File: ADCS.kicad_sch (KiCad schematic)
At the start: 14 parts

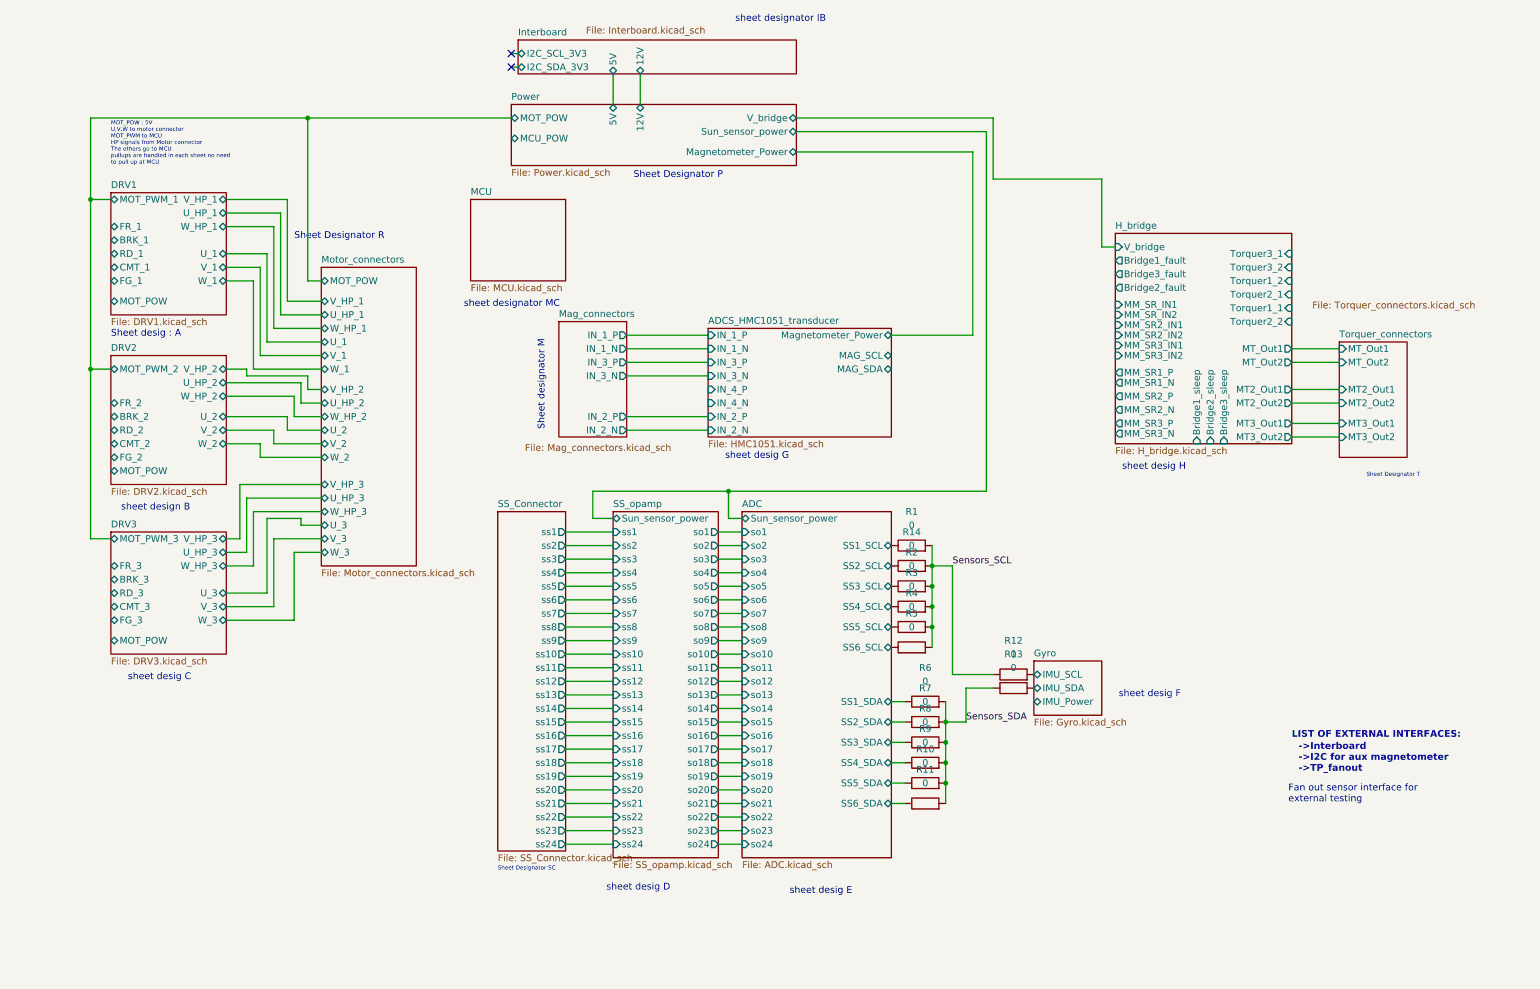
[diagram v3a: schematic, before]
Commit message: MCU interfaces pulled out to parent sheet
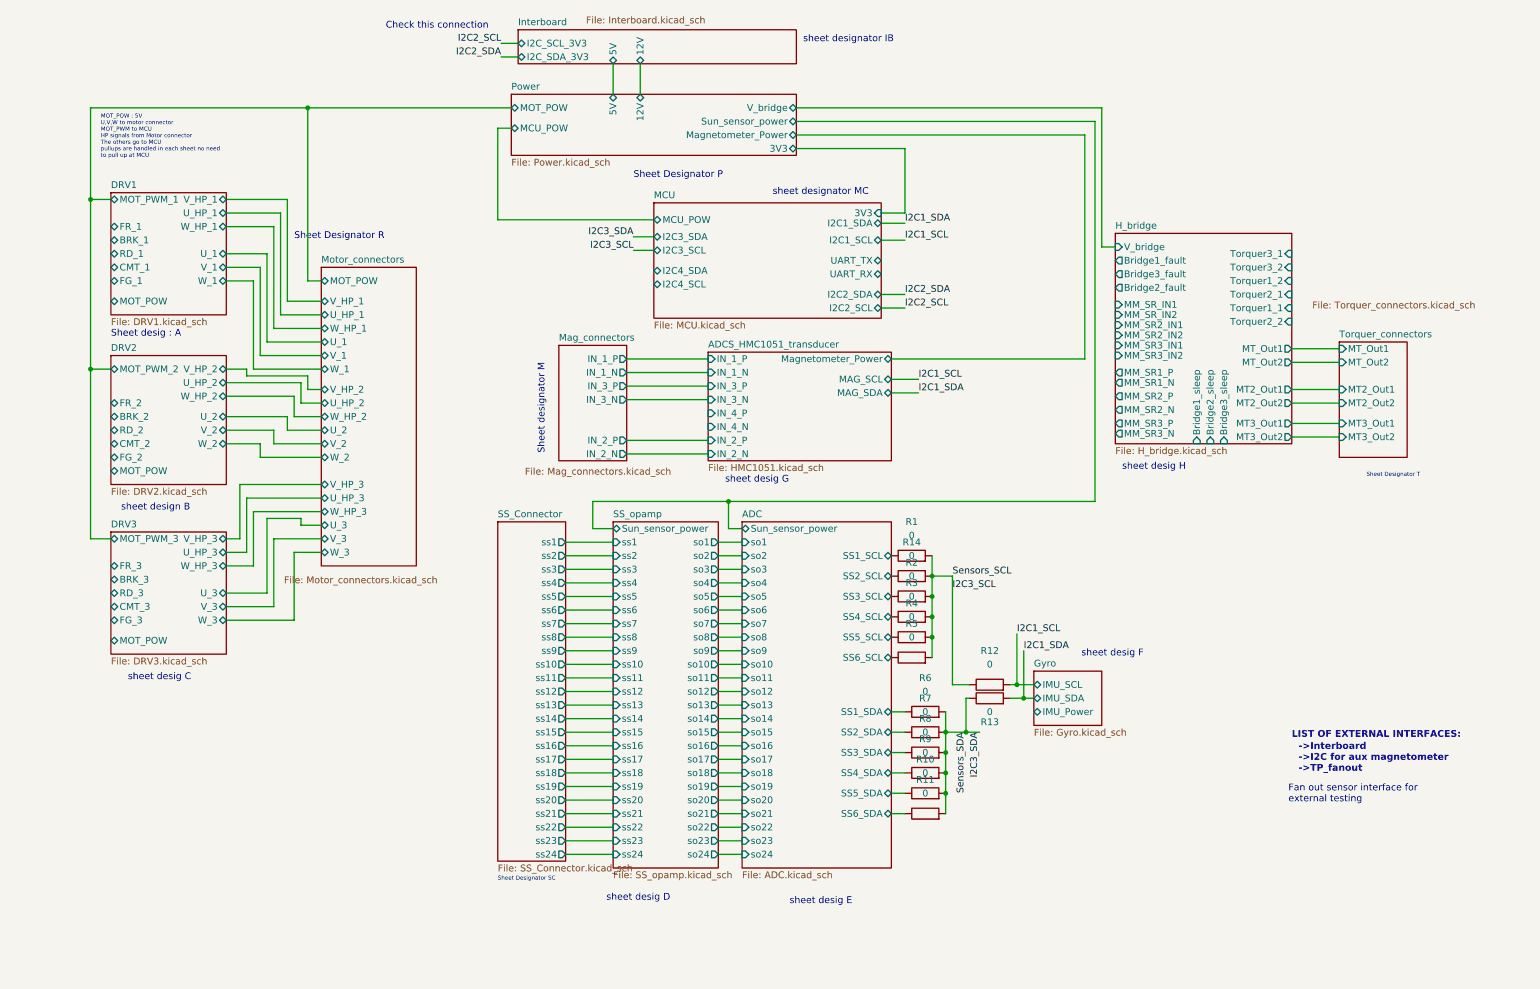
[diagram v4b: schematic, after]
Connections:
- net Gyro/IMU_SCL renamed I2C1_SCL
- net Gyro/IMU_SDA renamed I2C1_SDA
- net Sensors_SCL renamed I2C3_SCL
- net Sensors_SDA renamed I2C3_SDA
- no-connect marks 2 -> 0
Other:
- sheet MCU ports: added 3V3, I2C1_SCL, I2C1_SDA, I2C2_SCL, I2C2_SDA, I2C3_SCL, I2C3_SDA, I2C4_SCL, I2C4_SDA, MCU_POW, UART_RX, UART_TX; removed none
- sheet Power ports: added 3V3; removed none
- note added: "Check this connection"
- moved on the sheet: R1, R10, R11, R12, R13, R14, R2, R3, R4, R5, R6, R7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

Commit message: MCU interfaces are done! Check the Changes and Complete ERC modifications
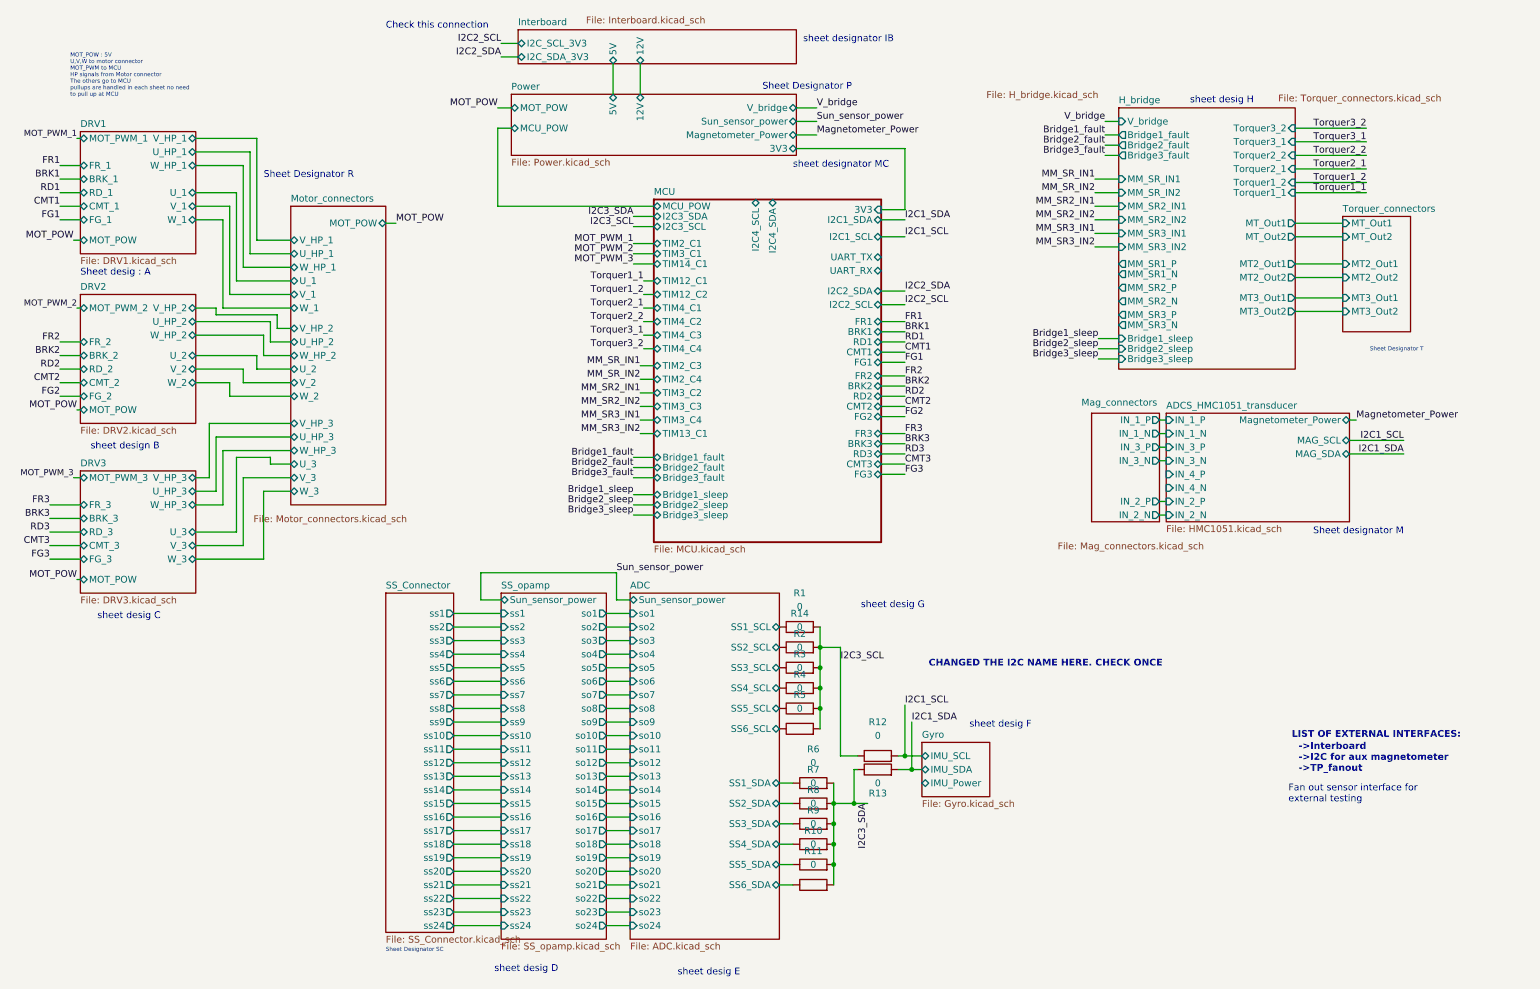
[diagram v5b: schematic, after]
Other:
- sheet MCU ports: added BRK1, BRK2, BRK3, Bridge1_fault, Bridge1_sleep, Bridge2_fault, Bridge2_sleep, Bridge3_fault, Bridge3_sleep, CMT1, CMT2, CMT3, FG1, FG2, FG3, FR1, FR2, FR3, RD1, RD2, RD3, TIM12_C1, TIM12_C2, TIM13_C1, TIM14_C1, TIM2_C1, TIM2_C3, TIM2_C4, TIM3_C1, TIM3_C2, TIM3_C3, TIM3_C4, TIM4_C1, TIM4_C2, TIM4_C3, TIM4_C4; removed none
- note added: "CHANGED THE I2C NAME HERE. CHECK ONCE"
- company: (none) -> Parikshit Student Satellite Team
- title: (none) -> AOCS BOARD
- moved on the sheet: R1, R10, R11, R12, R13, R14, R2, R3, R4, R5, R6, R7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

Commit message: added notes
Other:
- note added: "PWR flag for each power port ?"
- note added: "Please add necessary pull-ups for sensor buses Check each sheet for required pullups"
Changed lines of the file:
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@@
+    (effects (font (size 1.27 1.27)) (justify left bottom))
+  )
+  (text "PWR flag for each power port ? " (at 21.59 177.8 0)
     (effects (font (size 1.27 1.27)) (justify left bottom))
   )
@@
     (effects (font (size 0.762 0.762)) (justify left bottom))
   )
+  (text "Please add necessary \npull-ups \nfor sensor buses \nCheck each sheet for \nrequired pullups "
+    (at 21.59 172.72 0)
+    (effects (font (size 3.048 3.048)) (justify left bottom))
+  )
   (text "Fan out sensor interface for \nexternal testing \n" (at 249.555 161.29 0)

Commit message: Max ERC errors corrected
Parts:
- added RMCU? (x2): R, symbol Device:R
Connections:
- net I2C3_SCL: now also RMCU?.1
- net I2C3_SDA: now also RMCU?.1
- new net MCU_POW: RMCU?.2, RMCU?.2
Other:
- sheet DRV1 ports: added MCU_POW; removed none
- sheet DRV2 ports: added MCU_POW; removed none
- sheet DRV3 ports: added MCU_POW; removed none
- note added: "ADDED PULL UP Resistor at MCU for I2C3"

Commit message: Updated some comments
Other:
- note added: "What about these??"
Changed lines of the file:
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@@
     (effects (font (size 1.27 1.27)) (justify left bottom))
+  )
+  (text "What about these??" (at 196.85 65.405 0)
+    (effects (font (size 1.27 1.27) (thickness 0.254) bold italic) (justify left bottom))
   )
   (text "Sheet Designator R\n" (at 63.5 45.72 0)
